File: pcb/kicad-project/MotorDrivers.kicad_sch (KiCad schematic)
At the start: 10 parts, among them J3 Screw_Terminal_01x02, J4 Screw_Terminal_01x02, U3 DRV8871DDA, U4 DRV8871DDA

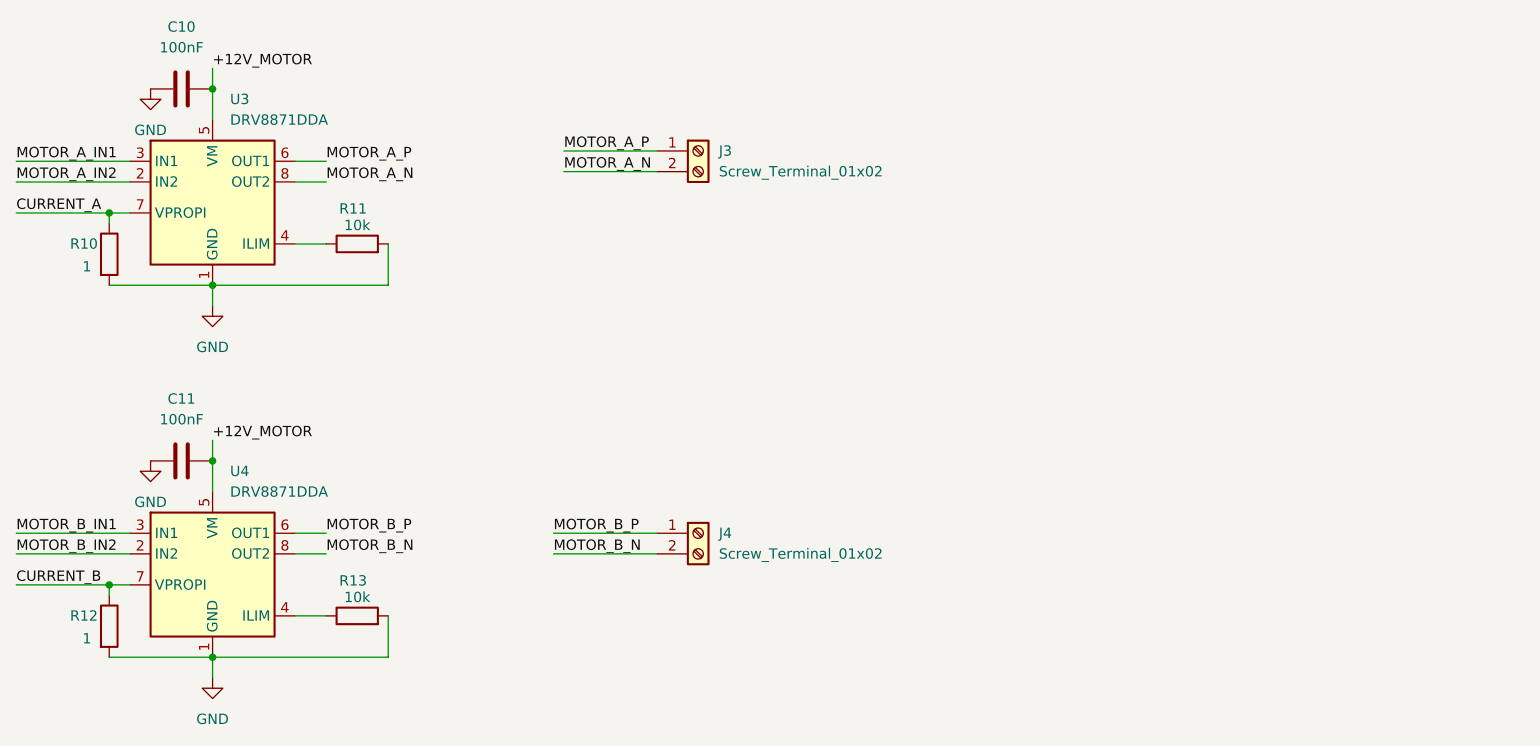
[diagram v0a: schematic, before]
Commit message: Added appropriate footprints to all components in the PCB
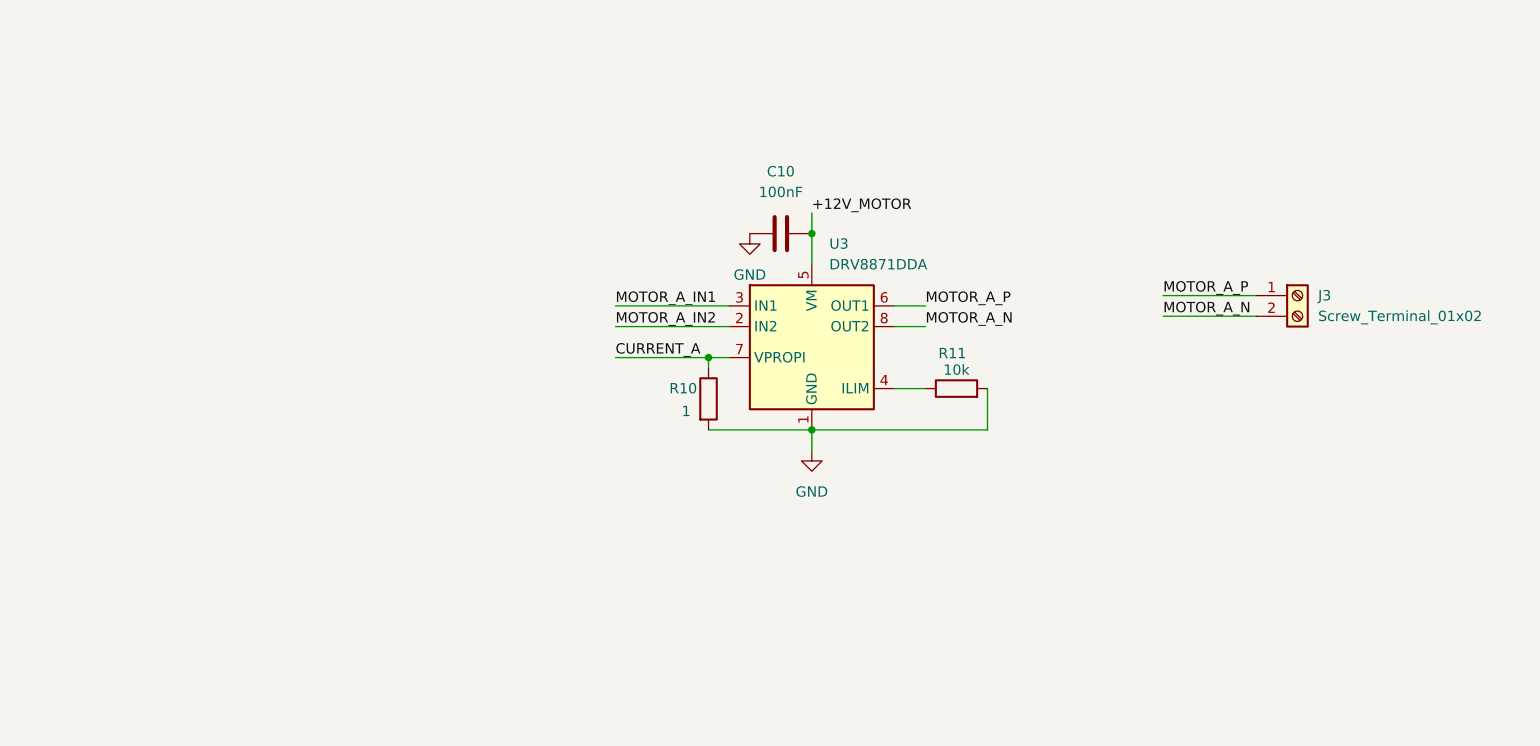
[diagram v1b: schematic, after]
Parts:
- removed C11: 100nF, symbol Device:C
- removed J4: Screw_Terminal_01x02, symbol Connector:Screw_Terminal_01x02
- removed R12: 1, symbol Device:R
- removed R13: 10k, symbol Device:R
- removed U4: DRV8871DDA, Package_SO:Texas_HTSOP-8-1EP_3.9x4.9mm_P1.27mm_EP2.95x4.9mm_Mask2.4x3.1mm_ThermalVias, symbol Driver_Motor:DRV8871DDA
- C10: footprint (none) -> Capacitor_SMD:C_0805_2012Metric
- J3: footprint (none) -> TerminalBlock_Phoenix:TerminalBlock_Phoenix_MKDS-1,5-2_1x02_P5.00mm_Horizontal
- R10, R11: footprint (none) -> Resistor_SMD:R_0805_2012Metric
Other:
- moved on the sheet: C10, J3, R10, R11, U3
